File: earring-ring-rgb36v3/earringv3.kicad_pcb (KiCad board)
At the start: 2 copper layers, 24 x 27.1 mm, 62 parts, among them J1 Conn_01x05, SW1 SW_Push, SW2 SW_Push, U1 STM32U073KCUx, U2 GMA2718H09-F42-4P

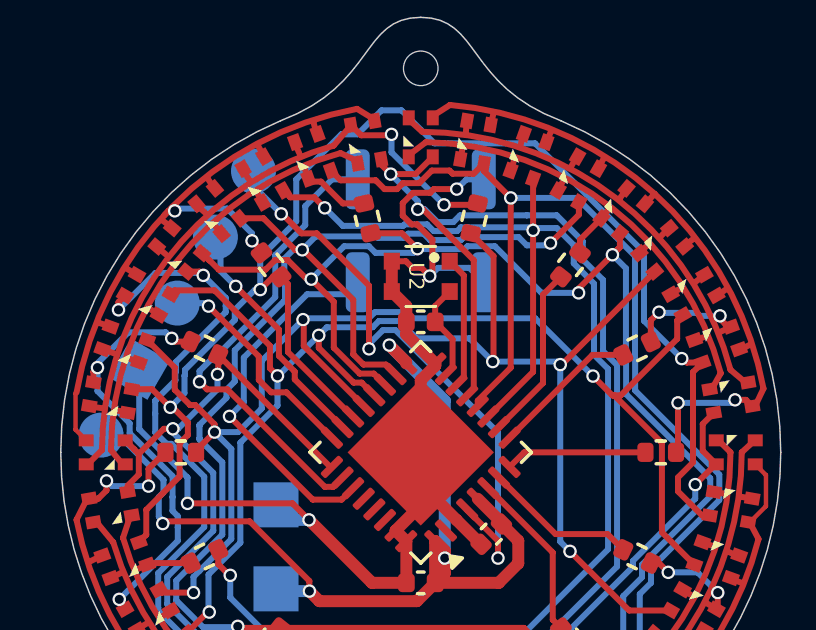
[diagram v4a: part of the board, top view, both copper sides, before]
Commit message: earring-ring-rgb36v3: add extra capacitor
The datasheet says this capacitor is needed so :shrug:
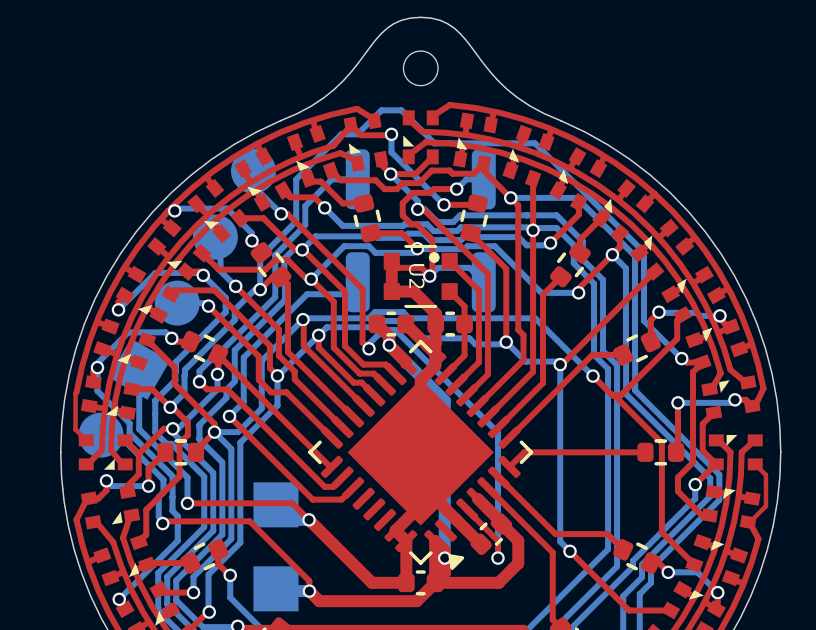
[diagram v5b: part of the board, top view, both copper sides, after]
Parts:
- added C4: 0.1uF, Capacitor_SMD:C_0402_1005Metric, F.Cu at (-0.98, -4.28)
- moved C2 0.98 mm to (0.98, -4.28)
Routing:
- net GND: track 40.4 -> 42.2 mm
- net VCC: track 33.6 -> 34.5 mm

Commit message: earring-ring-rgb36v3: prepare for ordering
  * Replace main MCU with a cheaper (in bulk) variant.
    (that is also in stock at JLCPCB)
  * Fix main MCU orientation (it's rotated differently at JLCPCB)
  * Replace red and green LED resistor with a higher value.
    Blue tends to be slightly dimmer, this might help with that.
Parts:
- R10, R11, R13, R4, R5, R6, R7, R8, R9: value 1.5k -> 2k
- U1: value STM32U073KCUx -> STM32U031K8Ux
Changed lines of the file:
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@@
 			)
 		)
-		(property "Value" "STM32U073KCUx"
+		(property "Value" "STM32U031K8Ux"
 			(at 0 3.83 135)
 			(layer "F.Fab")
@@
 			)
 		)
-		(property "Datasheet" "https://www.st.com/resource/en/datasheet/stm32u073kc.pdf"
+		(property "Datasheet" "https://www.st.com/resource/en/datasheet/stm32u031k8.pdf"
 			(at 0 0 135)
 			(layer "F.Fab")
@@
 			)
 		)
-		(property "Description" "STMicroelectronics Arm Cortex-M0+ MCU, 256KB flash, 40KB RAM, 56 MHz, 27 GPIO, UFQFPN32"
+		(property "Description" "STMicroelectronics Arm Cortex-M0+ MCU, 64KB flash, 12KB RAM, 27 GPIO, UFQFPN32"
 			(at 0 0 135)
 			(layer "F.Fab")
@@
 			)
 		)
-		(property "LCSC" "C22445363"
+		(property "LCSC" "C22445362"
 			(at 0 0 135)
 			(unlocked yes)
@@
 			)
 		)
+		(property "Rotation Offset" "270"
+			(at 0 0 0)
+			(unlocked yes)
+			(layer "F.Fab")
+			(hide yes)
+			(effects
+				(font
+					(size 1 1)
+					(thickness 0.15)
+				)
+			)
+		)
 		(property ki_fp_filters "QFN*1EP*5x5mm*P0.5mm*")
 		(sheetname "/")
@@
 			)
 		)
-		(property "Value" "1.5k"
+		(property "Value" "2k"
 			(at 0 1.17 102.86)
 			(layer "F.Fab")
@@
 			)
 		)
-		(property "LCSC" "C25867"
+		(property "LCSC" "C4109"
 			(at 0 0 282.86)
 			(unlocked yes)
@@
 			)
 		)
-		(property "Value" "1.5k"
+		(property "Value" "2k"
 			(at 0.000001 1.169999 102.86)
 			(layer "F.Fab")
@@
 			)
 		)
-		(property "LCSC" "C25867"
+		(property "LCSC" "C4109"
 			(at 0 0 102.86)
 			(unlocked yes)
@@
 			)
 		)
-		(property "Value" "1.5k"
+		(property "Value" "2k"
 			(at 0 1.17 77.14)
 			(layer "F.Fab")
@@
 			)
 		)
-		(property "LCSC" "C25867"
+		(property "LCSC" "C4109"
 			(at 0 0 257.14)
 			(unlocked yes)
@@
 			)
 		)
-		(property "Value" "1.5k"
+		(property "Value" "2k"
 			(at 0 1.17 154.29)
 			(layer "F.Fab")
@@
 			)
 		)
-		(property "LCSC" "C25867"
+		(property "LCSC" "C4109"
 			(at 0 0 334.29)
 			(unlocked yes)
@@
 			)
 		)
-		(property "Value" "1.5k"
+		(property "Value" "2k"
 			(at 0 1.17 51.43)
 			(layer "F.Fab")
@@
 			)
 		)
-		(property "LCSC" "C25867"
+		(property "LCSC" "C4109"
 			(at 0 0 51.43)
 			(unlocked yes)
@@
 			)
 		)
-		(property "Value" "1.5k"
+		(property "Value" "2k"
 			(at 0 1.17 51.43)
 			(layer "F.Fab")
@@
 			)
 		)
-		(property "LCSC" "C25867"
+		(property "LCSC" "C4109"
 			(at 0 0 231.43)
 			(unlocked yes)
@@
 			)
 		)
-		(property "Value" "1.5k"
+		(property "Value" "2k"
 			(at 0 1.17 25.71)
 			(layer "F.Fab")
@@
 			)
 		)
-		(property "LCSC" "C25867"
+		(property "LCSC" "C4109"
 			(at 0 0 25.71)
 			(unlocked yes)
@@
 			)
 		)
-		(property "Value" "1.5k"
+		(property "Value" "2k"
 			(at -0.000001 1.169999 77.14)
 			(layer "F.Fab")
@@
 			)
 		)
-		(property "LCSC" "C25867"
+		(property "LCSC" "C4109"
 			(at 0 0 77.14)
 			(unlocked yes)
@@
 			)
 		)
-		(property "Value" "1.5k"
+		(property "Value" "2k"
 			(at 0 1.17 25.71)
 			(layer "F.Fab")
@@
 			)
 		)
-		(property "LCSC" "C25867"
+		(property "LCSC" "C4109"
 			(at 0 0 205.71)
 			(unlocked yes)
